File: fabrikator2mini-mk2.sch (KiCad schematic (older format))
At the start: 81 parts, among them CON1 Micro_SD_Card, J1 USB_OTG, J10 END_X/ESP, J11 MT_Y, J12 Conn_01x12, J13 Z, J14 MT_Z, J15 B, J16 BTN1, J17 Fan1, J2 RESET, J3 PWR_IN, J4 B, J5 I2C, J6 SWD, J7 SPI, J8 Fan2, J9 MT_X, Q1 PSMN2R4-30MLD, Q2 PSMN2R4-30MLD, Q3 PSMN2R4-30MLD, Q4 PSMN2R4-30MLD, Q5 Si7145DP, U1 bluepill, U2 CPDT6-5V4, U3 CPDT6-5V4

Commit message: rc1 route
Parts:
- removed JP1: FAN1 PWR SEL, Pin_Headers:Pin_Header_Straight_1x03_Pitch2.54mm, symbol Jumper_NC_Dual
- removed JP2: FAN2 PWR SEL, Pin_Headers:Pin_Header_Straight_1x03_Pitch2.54mm, symbol Jumper_NC_Dual
- C1, C2, C21, C3, C4, C5, C6, C8: symbol C -> fabrikator2mini-mk2-rescue:C
- C20, C7: symbol CP1 -> fabrikator2mini-mk2-rescue:CP1
- CON1: symbol Micro_SD_Card -> fabrikator2mini-mk2-rescue:Micro_SD_Card
- D1, D10, D2, D3, D4, D6, D7, D8, D9: symbol LED -> fabrikator2mini-mk2-rescue:LED
- D5: symbol D_Zener -> fabrikator2mini-mk2-rescue:D_Zener
- F1: symbol Fuse_Small -> fabrikator2mini-mk2-rescue:Fuse_Small
- J1: symbol USB_OTG -> fabrikator2mini-mk2-rescue:USB_OTG
- J10, J6: symbol Conn_01x06 -> fabrikator2mini-mk2-rescue:Conn_01x06
- J11, J5, J9: symbol Conn_01x04 -> fabrikator2mini-mk2-rescue:Conn_01x04
- J12: symbol Conn_01x12 -> fabrikator2mini-mk2-rescue:Conn_01x12
- J13, J15, J16, J17, J2, J4, J8: symbol Conn_01x02 -> fabrikator2mini-mk2-rescue:Conn_01x02
- J14, J7: symbol Conn_01x05 -> fabrikator2mini-mk2-rescue:Conn_01x05
- J3: symbol Conn_01x03 -> fabrikator2mini-mk2-rescue:Conn_01x03
- Q1, Q2, Q3, Q4: symbol PSMN2R4-30MLD -> custom:PSMN2R4-30MLD
- Q5: symbol Si7145DP -> custom:Si7145DP
- R1, R10, R11, R12, R13, R14, R15, R16, R17, R18, R19, R2, R20, R21, R22, R23, R24, R25, R26, R3, R4, R40, R41, R42, R43, R44, R45, R5, R6, R7, R8, R9: symbol R -> fabrikator2mini-mk2-rescue:R
- U1: symbol bluepill -> custom:bluepill
- U2, U3: symbol CPDT6-5V4 -> custom:CPDT6-5V4
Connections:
- net VCC: now also J17.1 (Pin_1), J8.1 (Pin_1)

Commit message: fixed symbols after switch to kicad 5
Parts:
- C1, C2, C21, C3, C4, C5, C6, C8: symbol fabrikator2mini-mk2-rescue:C -> Device:C
- C20, C7: symbol fabrikator2mini-mk2-rescue:CP1 -> Device:CP1
- CON1: symbol fabrikator2mini-mk2-rescue:Micro_SD_Card -> Connector:Micro_SD_Card
- D1, D10, D2, D3, D4, D6, D7, D8, D9: symbol fabrikator2mini-mk2-rescue:LED -> Device:LED
- D5: symbol fabrikator2mini-mk2-rescue:D_Zener -> Device:D_Zener
- F1: symbol fabrikator2mini-mk2-rescue:Fuse_Small -> Device:Fuse_Small
- J1: symbol fabrikator2mini-mk2-rescue:USB_OTG -> Connector:USB_B_Micro
- J10, J6: symbol fabrikator2mini-mk2-rescue:Conn_01x06 -> Connector_Generic:Conn_01x06
- J11, J5, J9: symbol fabrikator2mini-mk2-rescue:Conn_01x04 -> Connector_Generic:Conn_01x04
- J12: symbol fabrikator2mini-mk2-rescue:Conn_01x12 -> Connector_Generic:Conn_01x12
- J13, J15, J16, J17, J2, J4, J8: symbol fabrikator2mini-mk2-rescue:Conn_01x02 -> Connector_Generic:Conn_01x02
- J14, J7: symbol fabrikator2mini-mk2-rescue:Conn_01x05 -> Connector_Generic:Conn_01x05
- J3: symbol fabrikator2mini-mk2-rescue:Conn_01x03 -> Connector_Generic:Conn_01x03
- R1, R10, R11, R12, R13, R14, R15, R16, R17, R18, R19, R2, R20, R21, R22, R23, R24, R25, R26, R3, R4, R40, R41, R42, R43, R44, R45, R5, R6, R7, R8, R9: symbol fabrikator2mini-mk2-rescue:R -> Device:R

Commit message: fixed modules after switch to kicad 5
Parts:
- C1, C2, C21, C3, C4, C5, C6, C8: footprint Capacitors_SMD:C_0805_HandSoldering -> Capacitor_SMD:C_0805_2012Metric_Pad1.15x1.40mm_HandSolder
- C20: footprint Capacitors_THT:CP_Radial_D10.0mm_P5.00mm -> Capacitor_THT:CP_Radial_D10.0mm_P5.00mm
- C7: footprint Capacitors_SMD:CP_Elec_8x10 -> Capacitor_SMD:CP_Elec_8x10
- CON1: footprint Connectors:microSD_Card_Receptacle_Wuerth_693072010801 -> Connector_Card:microSD_HC_Wuerth_693072010801
- D1, D10, D2, D3, D4, D6, D7, D8, D9: footprint LEDs:LED_0805 -> LED_SMD:LED_0805_2012Metric_Pad1.15x1.40mm_HandSolder
- D5: footprint Diodes_SMD:D_SOD-323 -> Diode_SMD:D_SOD-323_HandSoldering
- F1: footprint Fuse_Holders_and_Fuses:Fuseholder5x20_horiz_open_inline_Type-I -> Fuse:Fuseholder_Cylinder-5x20mm_Schurter_0031-8002_Horizontal_Open
- J1: footprint Connectors:USB_Micro-B -> Connector_USB:USB_Micro-B_Molex-105017-0001
- J10: footprint Connectors_JST:JST_PH_B6B-PH-K_06x2.00mm_Straight -> Connector_JST:JST_PH_B6B-PH-K_1x06_P2.00mm_Vertical
- J11, J5, J9: footprint Connectors_JST:JST_XH_B04B-XH-A_04x2.50mm_Straight -> Connector_JST:JST_XH_B04B-XH-A_1x04_P2.50mm_Vertical
- J12: footprint Connectors_JST:JST_PH_B12B-PH-K_12x2.00mm_Straight -> Connector_JST:JST_PH_B12B-PH-K_1x12_P2.00mm_Vertical
- J13, J4: footprint Connectors_JST:JST_XH_B02B-XH-A_02x2.50mm_Straight -> Connector_JST:JST_XH_B02B-XH-A_1x02_P2.50mm_Vertical
- J14, J7: footprint Connectors_JST:JST_XH_B05B-XH-A_05x2.50mm_Straight -> Connector_JST:JST_XH_B05B-XH-A_1x05_P2.50mm_Vertical
- J15: footprint Connectors_Molex:Molex_KK-41791-02_02x3.96mm_Straight -> Connector_Hirose:Hirose_DF63-2P-3.96DSA_1x02_P3.96mm_Horizontal
- J16: footprint Buttons_Switches_THT:SW_Tactile_SPST_Angled_PTS645Vx58-2LFS -> Button_Switch_THT:SW_Tactile_SPST_Angled_PTS645Vx58-2LFS
- J17, J8: footprint Connectors_JST:JST_PH_B2B-PH-K_02x2.00mm_Straight -> Connector_JST:JST_PH_B2B-PH-K_1x02_P2.00mm_Vertical
- J2: footprint Buttons_Switches_SMD:SW_SPST_B3S-1000 -> Button_Switch_SMD:SW_SPST_B3S-1000
- J3: footprint Connectors_Molex:Molex_KK-41791-03_03x3.96mm_Straight -> Connector_Hirose:Hirose_DF63-3P-3.96DSA_1x03_P3.96mm_Horizontal
- Q1, Q2, Q3, Q4: footprint TO_SOT_Packages_SMD:LFPAK33 -> Package_TO_SOT_SMD:LFPAK33
- Q5: footprint SMD_Packages:SO-8_PowerPAK_Vishay_Single -> Package_SO:PowerPAK_SO-8_Single
- R1, R10, R11, R12, R13, R14, R15, R16, R17, R18, R19, R2, R20, R21, R22, R23, R24, R25, R26, R3, R4, R40, R41, R42, R43, R44, R45, R5, R6, R7, R8, R9: footprint Resistors_SMD:R_0805_HandSoldering -> Resistor_SMD:R_0805_2012Metric_Pad1.15x1.40mm_HandSolder
- U2, U3: footprint TO_SOT_Packages_SMD:SOT-23-6_Handsoldering -> Package_TO_SOT_SMD:SOT-23-6_Handsoldering

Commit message: fixed symbols after switch to kicad 5
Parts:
- F1: footprint Fuse:Fuseholder_Cylinder-5x20mm_Schurter_0031-8002_Horizontal_Open -> Fuse:Fuseholder_Cylinder-5x20mm_Schurter_0031_8201_Horizontal_Open
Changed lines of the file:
@@
 F 0 "F1" H 4000 4490 50  0000 C CNN
 F 1 "15A" H 4000 4610 50  0000 C CNN
-F 2 "Fuse:Fuseholder_Cylinder-5x20mm_Schurter_0031-8002_Horizontal_Open" H 4000 4550 50  0001 C CNN
+F 2 "Fuse:Fuseholder_Cylinder-5x20mm_Schurter_0031_8201_Horizontal_Open" H 4000 4550 50  0001 C CNN
 F 3 "" H 4000 4550 50  0000 C CNN
 	1    4000 4550

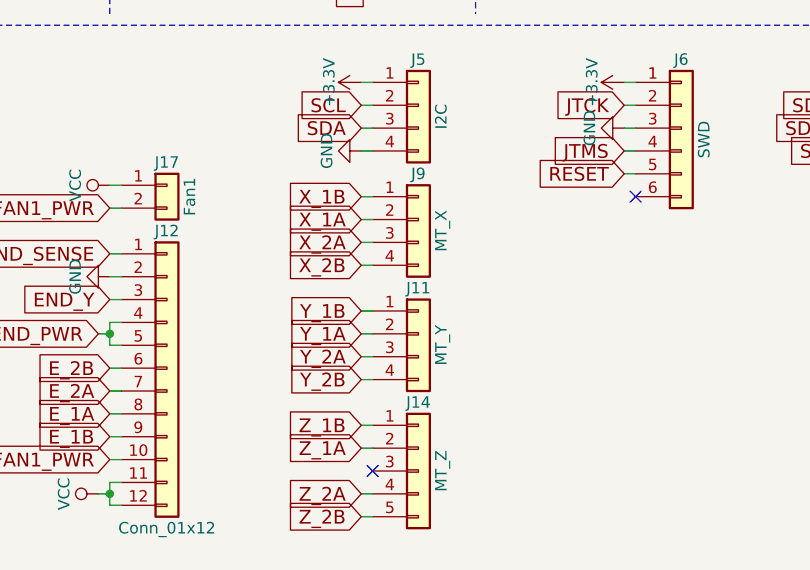
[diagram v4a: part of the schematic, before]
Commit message: rotated X Y Z connectos to correct orientation
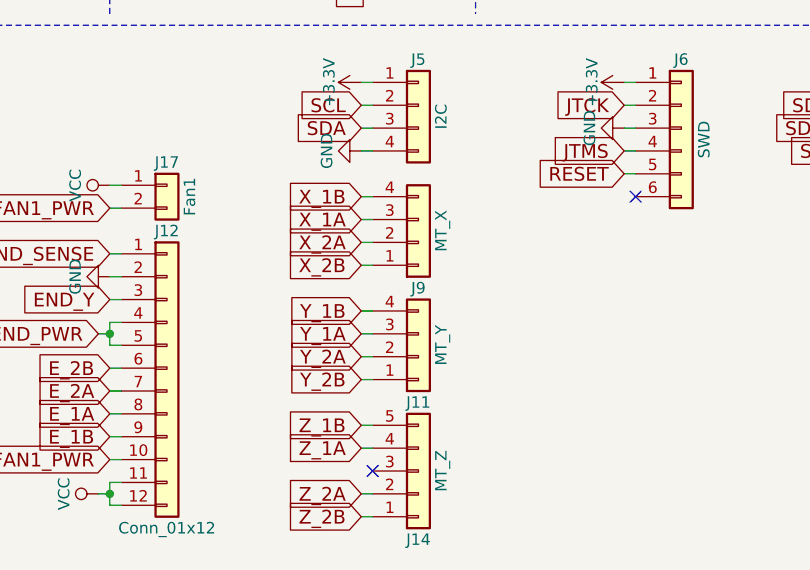
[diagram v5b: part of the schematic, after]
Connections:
- net X_1A: now also J9.3 (Pin_3); no longer J9.2 (Pin_2)
- net X_1B: now also J9.4 (Pin_4); no longer J9.1 (Pin_1)
- net X_2A: now also J9.2 (Pin_2); no longer J9.3 (Pin_3)
- net X_2B: now also J9.1 (Pin_1); no longer J9.4 (Pin_4)
- net Y_1A: now also J11.3 (Pin_3); no longer J11.2 (Pin_2)
- net Y_1B: now also J11.4 (Pin_4); no longer J11.1 (Pin_1)
- net Y_2A: now also J11.2 (Pin_2); no longer J11.3 (Pin_3)
- net Y_2B: now also J11.1 (Pin_1); no longer J11.4 (Pin_4)
- net Z_1A: now also J14.4 (Pin_4); no longer J14.2 (Pin_2)
- net Z_1B: now also J14.5 (Pin_5); no longer J14.1 (Pin_1)
- net Z_2A: now also J14.2 (Pin_2); no longer J14.4 (Pin_4)
- net Z_2B: now also J14.1 (Pin_1); no longer J14.5 (Pin_5)
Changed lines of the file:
@@
 F 3 "" H 6750 7500 50  0001 C CNN
 	1    6750 7500
-	1    0    0    -1
+	1    0    0    1
 $EndComp
 $Comp
@@
 L Connector_Generic:Conn_01x04 J9
 U 1 1 5A7E611B
-P 6750 6400
-F 0 "J9" H 6750 6600 50  0000 C CNN
-F 1 "MT_X" V 6850 6350 50  0000 C CNN
-F 2 "Connector_JST:JST_XH_B04B-XH-A_1x04_P2.50mm_Vertical" H 6750 6400 50  0001 C CNN
-F 3 "" H 6750 6400 50  0001 C CNN
-	1    6750 6400
-	1    0    0    -1
+P 6750 6500
+F 0 "J9" H 6750 6700 50  0000 C CNN
+F 1 "MT_X" V 6850 6450 50  0000 C CNN
+F 2 "Connector_JST:JST_XH_B04B-XH-A_1x04_P2.50mm_Vertical" H 6750 6500 50  0001 C CNN
+F 3 "" H 6750 6500 50  0001 C CNN
+	1    6750 6500
+	1    0    0    1
 $EndComp
 $Comp
 L Connector_Generic:Conn_01x04 J11
 U 1 1 5A7E62E2
-P 6750 6900
-F 0 "J11" H 6750 7100 50  0000 C CNN
-F 1 "MT_Y" V 6850 6850 50  0000 C CNN
-F 2 "Connector_JST:JST_XH_B04B-XH-A_1x04_P2.50mm_Vertical" H 6750 6900 50  0001 C CNN
-F 3 "" H 6750 6900 50  0001 C CNN
-	1    6750 6900
-	1    0    0    -1
+P 6750 7000
+F 0 "J11" H 6750 7200 50  0000 C CNN
+F 1 "MT_Y" V 6850 6950 50  0000 C CNN
+F 2 "Connector_JST:JST_XH_B04B-XH-A_1x04_P2.50mm_Vertical" H 6750 7000 50  0001 C CNN
+F 3 "" H 6750 7000 50  0001 C CNN
+	1    6750 7000
+	1    0    0    1
 $EndComp
 $Comp
